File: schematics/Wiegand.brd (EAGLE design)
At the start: 78.7 x 58.4 mm, 67 parts, among them J1 AVR_SPI_PRG_6NS, Q1 NTR1P02T1G, Q2 NTR1P02T1G, U1 ATMEGA168, U2 RS485_SP491, U4 MOC3063, U5 MOC3063, U6 MOC3063, U7 MOC3063, U8 MOC3063, U9 MOC3063, Y1 16Mhz

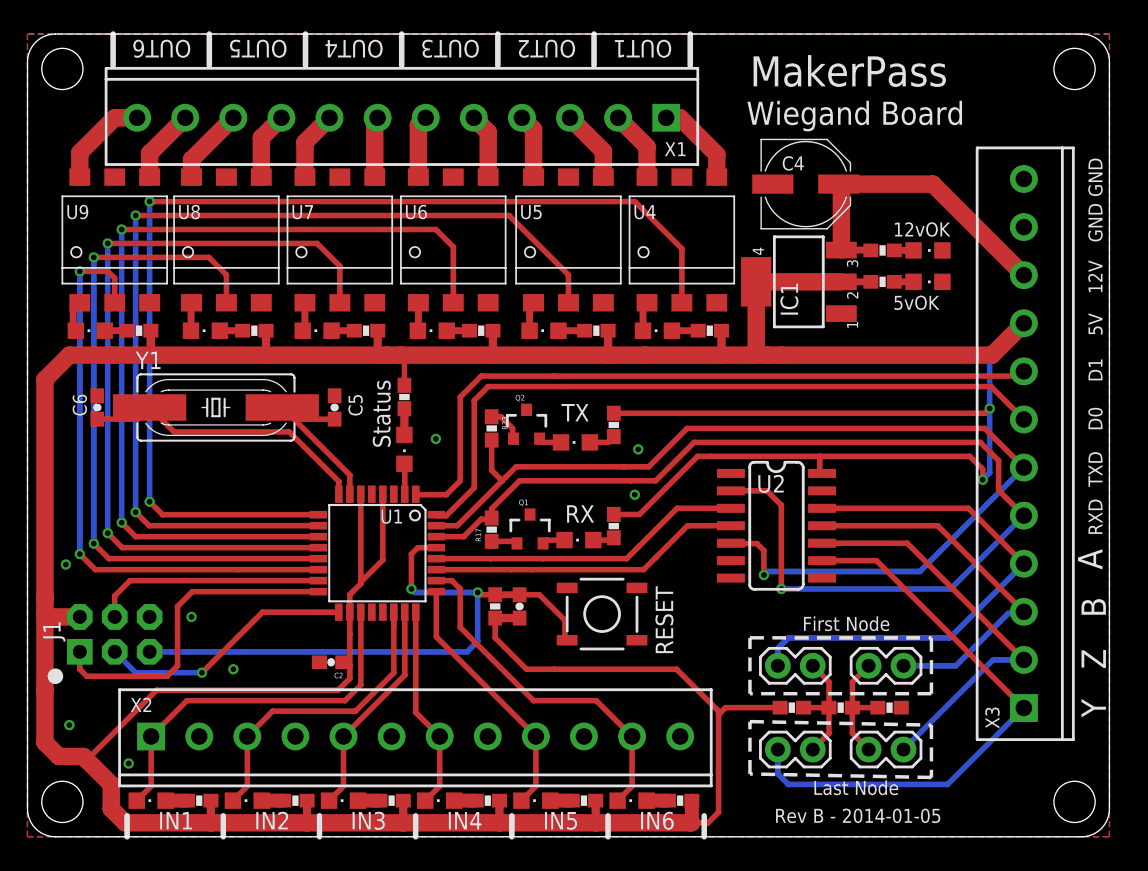
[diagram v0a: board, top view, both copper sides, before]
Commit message: minor edits to brd, rerendered eagleup model
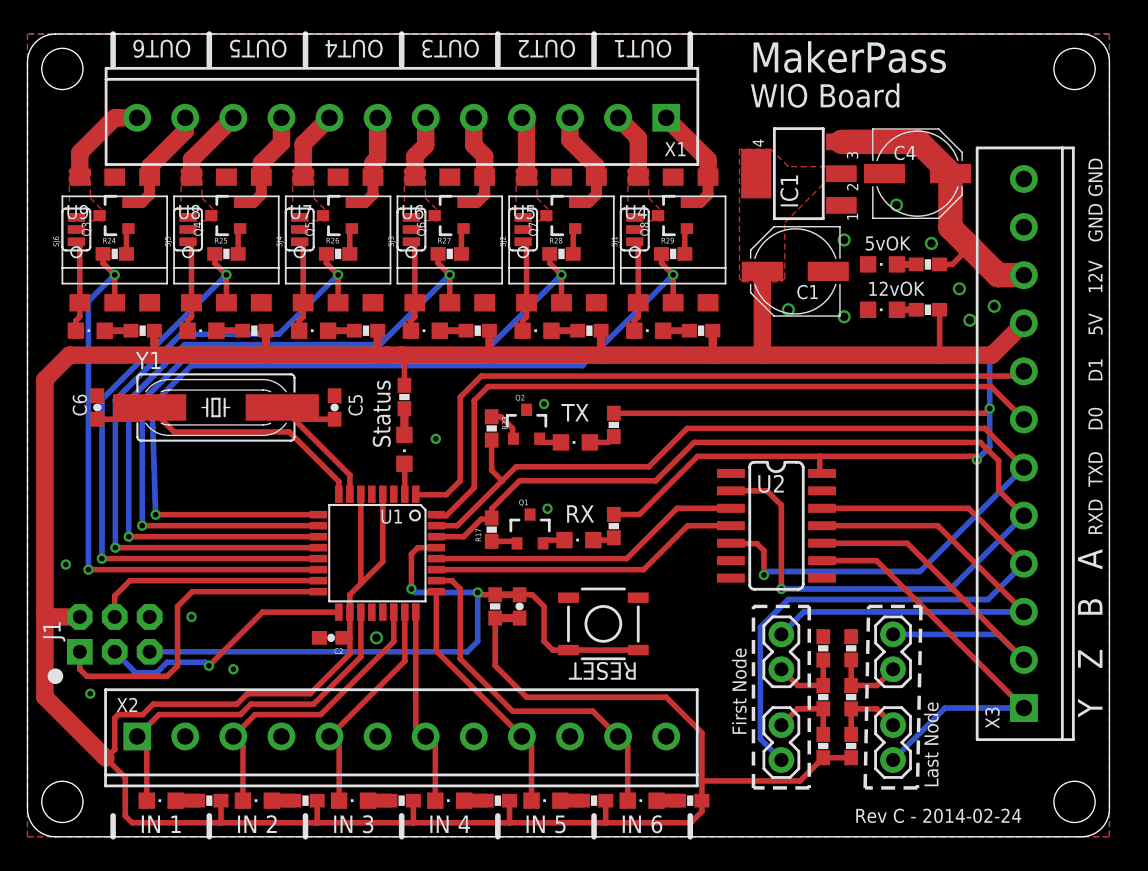
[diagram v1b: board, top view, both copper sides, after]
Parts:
- added C1: 10uF, rcl:PANASONIC_D
- added Q3, Q4, Q5, Q6, Q7, Q8: (no value), LumisenseV6:SOT23-3
- added R24, R25, R26, R27, R28, R29, R31, R32: 1K, SparkFun:0603-RES
- added R30: 100, SparkFun:0603-RES
- added SJ1, SJ2, SJ3, SJ4, SJ5, SJ6: (no value), SparkFun-Passives:SJ_3
- C4: value 47uF -> 10uF
- moved JP4 9.18 mm to (54.9, 14.7), turned to 270 degrees
- moved LED12 8.76 mm to (37.1, 36.8)
- moved C4 8.16 mm to (64.8, 48.3)
- moved IC1 7.87 mm to (56.1, 48.3)
- moved LED11 7.62 mm to (45.2, 36.8)
- moved JP2 6.86 mm to (54.9, 5.59), turned to 90 degrees
- moved R16 6.48 mm to (57.9, 13.7), turned to 270 degrees
- moved JP5 6.11 mm to (63.0, 12.2), turned to 90 degrees
- moved JP3 6.11 mm to (63.0, 8.13), turned to 270 degrees
- moved LED1 3.88 mm to (62.2, 38.4), turned to 90 degrees
- moved R13 3.88 mm to (65.5, 38.4), turned to 0 degrees
- moved R14 3.61 mm to (57.9, 6.60), turned to 270 degrees
- moved LED4 3.45 mm to (62.2, 41.7), turned to 90 degrees
- moved R18 3.45 mm to (65.5, 41.7), turned to 0 degrees
- moved C2 1.78 mm to (22.1, 14.5)
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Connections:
- removed net N$17: U4.4, X1.1
- new net N$43: Q4.1, R25.2
- new net N$435: Q3.1, R24.2
- new net N$44: Q5.1, R26.2
- new net N$48: Q6.1, R27.2
- new net N$49: Q7.1, R28.2
- new net N$50: Q8.1, R29.2
- new net N$51: JP2.2, R14.1, R15.2
- new net N$52: JP4.2, R15.1, R16.2
- new net N$53: Q8.2, U4.4, X1.1
- net GND: now also C1.-, R32.1, S2.3, SJ1.2, SJ2.2, SJ3.2, SJ4.2, SJ5.2, SJ6.2
- net N$15: now also LED11.C, SJ1.1; no longer LED12.C
- net N$16: now also LED11.A; no longer LED12.A
- net N$18: now also Q8.3, SJ1.3
- net N$19: now also Q7.2
- net N$20: now also Q7.3, SJ2.3
- net N$21: now also LED12.A; no longer LED11.A
- net N$22: now also LED12.C, SJ2.1; no longer LED11.C
- net N$23: now also Q6.2
- net N$24: now also Q6.3, SJ3.3
- net N$28: now also SJ3.1
- net N$29: now also Q5.2
- net N$3: now also Q4.2
- net N$30: now also Q5.3, SJ4.3
- net N$32: now also SJ4.1
- net N$36: now also SJ5.1
- net N$37: now also Q3.3, SJ6.3, U9.6, X1.12; no longer U9.4, X1.11
- net N$38: now also Q3.2, U9.4, X1.11; no longer U9.6, X1.12
- net N$4: now also Q4.3, SJ5.3
- net N$40: now also SJ6.1
- net N$6: now also R30.1, R32.2; no longer JP4.2, R15.1, R16.2
- net N$7: now also R30.2, R31.1; no longer JP2.2, R14.1, R15.2
- net OUTPUT1: now also R29.1
- net OUTPUT2: now also R28.1
- net OUTPUT3: now also R27.1
- net OUTPUT4: now also R26.1
- net OUTPUT5: now also R25.1
- net OUTPUT6: now also R24.1
- net RESET: now also S2.1
- net VCC: now also C1.+, R31.2
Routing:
- net OUTPUT1: track 78.6 -> 65.6 mm
- net RS485-Y: track 41.4 -> 30.2 mm
- net OUTPUT2: track 70.6 -> 60.1 mm
- net OUTPUT3: track 64.8 -> 54.8 mm
- net RS485-A: track 38.1 -> 47.7 mm
- net N$53: track 0.00 -> 8.63 mm
- net RS485-B: track 27.7 -> 35.6 mm
- net OUTPUT4: track 57.1 -> 49.4 mm
- net VCC: track 342.5 -> 335.6 mm
- net N$17: track 6.44 -> 0.00 mm
- net RESET: track 45.9 -> 52.1 mm
- net OUTPUT5: track 49.8 -> 44.1 mm
- net N$51: track 0.00 -> 5.39 mm
- net N$52: track 0.00 -> 5.39 mm
- net N$36: track 2.05 -> 6.70 mm
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- added copper zone on layer 1, net N$18
- added copper zone on layer 1, net N$20
- added copper zone on layer 1, net N$24
- added copper zone on layer 1, net N$30
- added copper zone on layer 1, net N$37
- added copper zone on layer 1, net N$4
- added copper zone on layer 1, net VCC
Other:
- board text added: "IN 1"
- board text added: "IN 2"
- board text added: "IN 3"
- board text added: "IN 4"
- board text added: "IN 5"
- board text added: "IN 6"
- board text added: "Rev C - 2014-02-24"
- board text added: "WIO Board"
- board text removed: "IN1"
- board text removed: "IN2"
- board text removed: "IN3"
- board text removed: "IN4"
- board text removed: "IN5"
- board text removed: "IN6"
- board text removed: "Rev B - 2014-01-05"
- board text removed: "Wiegand Board"
